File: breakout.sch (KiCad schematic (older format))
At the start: 20 parts, among them P1 CONN_01X08, P2 SPEAKER, P3 ISO7816_SIMPLE, P4 CONN_01X04, P5 SMA_CONN, P6 CONN_01X08, Q1 Q_PMOS_GSD, Q2 Q_NMOS_GSD, U1 SPX3819, U2 ESP-12E

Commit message: More stuff.
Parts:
- removed P4: CONN_01X04, Pin_Headers:Pin_Header_Straight_1x04, symbol CONN_01X04
- removed P6: CONN_01X08, Pin_Headers:Pin_Header_Straight_1x08, symbol CONN_01X08
- added J1: JACK_TRS_4PINS, Misc:PJ-320L, symbol JACK_TRS_4PINS
- added P4: CONN_01X09, Pin_Headers:Pin_Header_Straight_1x09, symbol CONN_01X09
- added P7: USB_A, Connect:USB_Micro-B_10103594-0001LF, symbol USB_A
- C3: value 470 uF -> 100 uF; footprint Capacitors_ThroughHole:C_Radial_D8_L13_P3.8 -> Capacitors_Tantalum_SMD:TantalC_SizeB_EIA-3528_HandSoldering
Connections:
- net labels added: ADC, CH_PD, EARL, EARR, GPIO0, GPIO12, GPIO13, GPIO14, GPIO16, GPIO2, GPIO4, GPIO5, MIC+, REST, RX, TX
- wire segments 147 -> 118
- no-connect marks 25 -> 27
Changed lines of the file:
@@
 LIBS:SIMtrace
 LIBS:smartcard
+LIBS:misc
+LIBS:nodemcu
+LIBS:sensors
 LIBS:breakout-cache
 EELAYER 25 0
@@
 P 6000 4850
 F 0 "C3" H 6025 4950 50  0000 L CNN
-F 1 "470 uF" H 6025 4750 50  0000 L CNN
-F 2 "Capacitors_ThroughHole:C_Radial_D8_L13_P3.8" H 6038 4700 50  0001 C CNN
+F 1 "100 uF" H 6025 4750 50  0000 L CNN
+F 2 "Capacitors_Tantalum_SMD:TantalC_SizeB_EIA-3528_HandSoldering" H 6038 4700 50  0001 C CNN
 F 3 "" H 6000 4850 50  0000 C CNN
 	1    6000 4850
@@
 NoConn ~ 2900 5550
 NoConn ~ 2900 5650
-$Comp
-L CONN_01X04 P4
-U 1 1 57B00DE5
-P 3750 7300
-F 0 "P4" H 3750 7550 50  0000 C CNN
-F 1 "CONN_01X04" V 3850 7300 50  0000 C CNN
-F 2 "Pin_Headers:Pin_Header_Straight_1x04" H 3750 7300 50  0001 C CNN
-F 3 "" H 3750 7300 50  0000 C CNN
-	1    3750 7300
-	0    1    1    0
-$EndComp
-NoConn ~ 2900 6350
 NoConn ~ 2900 6550
 $Comp
@@
 $EndComp
 $Comp
-L GND #PWR012
+L GND #PWR011
 U 1 1 57B7110B
 P 9000 4550
-F 0 "#PWR012" H 9000 4300 50  0001 C CNN
+F 0 "#PWR011" H 9000 4300 50  0001 C CNN
 F 1 "GND" H 9000 4400 50  0000 C CNN
 F 2 "" H 9000 4550 50  0000 C CNN
@@
 	1750 1350 1750 1250
 Wire Wire Line
-	4100 1750 4700 1750
-Wire Wire Line
-	4700 1750 4800 1750
-Wire Wire Line
-	4100 1950 4350 1950
-Wire Wire Line
-	4350 1950 4800 1950
-Wire Wire Line
-	4100 2150 4550 2150
-Wire Wire Line
-	4550 2150 4800 2150
-Wire Wire Line
-	4100 2250 4450 2250
-Wire Wire Line
-	4450 2250 4800 2250
-Wire Wire Line
-	6600 2150 6650 2150
-Wire Wire Line
-	6650 2150 7250 2150
-Wire Wire Line
-	6600 2250 7000 2250
-Wire Wire Line
-	7000 2250 7250 2250
-Wire Wire Line
-	6600 2350 6900 2350
-Wire Wire Line
-	6900 2350 7150 2350
-Wire Wire Line
-	7150 2350 7250 2350
+	4100 1750 4800 1750
+Wire Wire Line
+	4100 1950 4800 1950
+Wire Wire Line
+	4100 2150 4800 2150
+Wire Wire Line
+	4100 2250 4800 2250
+Wire Wire Line
+	6600 2150 7250 2150
+Wire Wire Line
+	6600 2250 7250 2250
+Wire Wire Line
+	6600 2350 7250 2350
 Wire Wire Line
 	6600 2450 6650 2450
 Wire Wire Line
-	3650 950  3850 950
-Wire Wire Line
-	3850 950  4200 950
-Wire Wire Line
-	4200 950  4350 950
-Wire Wire Line
-	4350 950  4700 950
-Wire Wire Line
-	4700 950  6650 950
-Wire Wire Line
-	6650 950  7000 950
-Wire Wire Line
-	3200 1300 3200 1550
-Wire Wire Line
-	3200 1550 3200 3050
-Wire Wire Line
-	3200 3050 6650 3050
-Wire Wire Line
-	6650 3050 6900 3050
-Wire Wire Line
-	6900 3050 7250 3050
+	3650 950  7000 950
+Wire Wire Line
+	3200 1300 3200 3050
+Wire Wire Line
+	2400 3050 7250 3050
 Wire Wire Line
 	4350 1450 4350 1950
@@
 	5650 5150 5400 5150
 Wire Wire Line
-	5400 4850 5650 4850
-Wire Wire Line
-	5650 4850 5850 4850
+	5400 4850 5850 4850
 Wire Wire Line
 	5400 4750 5650 4750
@@
 	5650 4650 5650 4550
 Wire Wire Line
-	5400 4550 5650 4550
-Wire Wire Line
-	5650 4550 6200 4550
-Wire Wire Line
-	6200 4550 6300 4550
+	5400 4550 6300 4550
 Wire Wire Line
 	6200 4550 6200 4850
@@
 Connection ~ 5650 6550
 Wire Wire Line
-	2500 5000 2500 5100
-Wire Wire Line
-	2500 5100 2500 5750
-Wire Wire Line
-	2500 5750 2500 6250
-Wire Wire Line
-	2500 6250 2500 6350
+	2500 5000 2500 6350
 Wire Wire Line
 	2500 5750 2900 5750
@@
 Wire Wire Line
 	6100 5250 5400 5250
-Wire Wire Line
-	3700 7100 3700 6850
-Wire Wire Line
-	3700 6850 5450 6850
-Wire Wire Line
-	5450 6850 5450 6650
-Wire Wire Line
-	5650 6650 5450 6650
-Connection ~ 5650 6650
-Wire Wire Line
-	5400 6350 5550 6350
-Wire Wire Line
-	5550 6350 5550 6950
-Wire Wire Line
-	5550 6950 3800 6950
-Wire Wire Line
-	3800 6950 3800 7100
-Wire Wire Line
-	3900 7100 5600 7100
-Wire Wire Line
-	5600 7100 5600 6450
-Wire Wire Line
-	5600 6450 5400 6450
-Wire Wire Line
-	3600 7100 2800 7100
-Wire Wire Line
-	2800 7100 2800 6450
-Wire Wire Line
-	2800 6450 2900 6450
 Wire Wire Line
 	1000 5200 1000 5200
@@
 	6100 5350 6100 5400
 Wire Wire Line
-	5650 4750 5650 4850
-Wire Wire Line
-	5650 4850 5650 5150
-Wire Wire Line
-	5650 5150 5650 5350
-Wire Wire Line
-	5650 5350 5650 5950
-Wire Wire Line
-	5650 5950 5650 6250
-Wire Wire Line
-	5650 6250 5650 6550
-Wire Wire Line
-	5650 6550 5650 6650
-Wire Wire Line
-	5650 6650 5650 7150
+	5650 4750 5650 7150
 Wire Wire Line
 	7250 3050 7250 2450
 Wire Wire Line
-	2500 6250 2900 6250
+	2300 6250 2900 6250
 Wire Wire Line
 	2900 5250 2850 5250
@@
 	5400 6150 5850 6150
 Wire Wire Line
-	2650 850  2650 950
-Wire Wire Line
-	2650 950  2650 1100
-Wire Wire Line
-	2650 1100 2650 2600
+	2650 850  2650 2600
 Wire Wire Line
 	2650 950  2750 950
@@
 Connection ~ 7150 2350
 Wire Wire Line
-	9450 3550 9450 3600
-Wire Wire Line
-	9450 3600 9450 3750
+	9450 3550 9450 3750
 Wire Wire Line
 	9450 3600 9000 3600
 Connection ~ 9450 3600
 Wire Wire Line
-	9000 3900 9000 3950
-Wire Wire Line
-	9000 3950 9000 4050
+	9000 3900 9000 4050
 Wire Wire Line
 	9000 3950 9150 3950
@@
 Wire Wire Line
 	9450 4250 9850 4250
-$Comp
-L CONN_01X08 P6
-U 1 1 57B536C2
-P 3900 2100
-F 0 "P6" H 3900 2550 50  0000 C CNN
-F 1 "CONN_01X08" V 4000 2100 50  0000 C CNN
-F 2 "Pin_Headers:Pin_Header_Straight_1x08" H 3900 2100 50  0001 C CNN
-F 3 "" H 3900 2100 50  0000 C CNN
-	1    3900 2100
+Wire Wire Line
+	2650 2600 4100 2600
+Connection ~ 2650 1100
+$Comp
+L USB_A P7
+U 1 1 57B79205
+P 1800 1950
+F 0 "P7" H 2000 1750 50  0000 C CNN
+F 1 "USB_A" H 1750 2150 50  0000 C CNN
+F 2 "Connect:USB_Micro-B_10103594-0001LF" V 1750 1850 50  0001 C CNN
+F 3 "" V 1750 1850 50  0000 C CNN
+	1    1800 1950
+	0    -1   -1   0
+$EndComp
+Wire Wire Line
+	2100 2150 2650 2150
+Connection ~ 2650 2150
+Wire Wire Line
+	2100 1850 2400 1850
+Wire Wire Line
+	2400 1850 2400 3050
+Connection ~ 3200 3050
+NoConn ~ 2100 1950
+NoConn ~ 2100 2050
+NoConn ~ 1700 1650
+Wire Wire Line
+	2900 6350 2850 6350
+Wire Wire Line
+	2850 6350 2850 6250
+Connection ~ 2850 6250
+$Comp
+L JACK_TRS_4PINS J1
+U 1 1 57B7BE51
+P 1650 7250
+F 0 "J1" H 1650 7650 50  0000 C CNN
+F 1 "JACK_TRS_4PINS" H 1600 6950 50  0000 C CNN
+F 2 "Misc:PJ-320L" H 1750 7100 50  0001 C CNN
+F 3 "" H 1750 7100 50  0000 C CNN
+	1    1650 7250
+	1    0    0    -1
+$EndComp
+Wire Wire Line
+	2900 6450 2750 6450
+Wire Wire Line
+	2750 6450 2750 6950
+Wire Wire Line
+	2750 6950 2150 6950
+Wire Wire Line
+	2150 7050 2300 7050
+Wire Wire Line
+	2300 7050 2300 6250
+Wire Wire Line
+	5400 6450 5450 6450
+Wire Wire Line
+	5450 6450 5450 7250
+Wire Wire Line
+	5450 7250 2150 7250
+Wire Wire Line
+	2150 7450 5550 7450
+Wire Wire Line
+	5550 7450 5550 6350
+Wire Wire Line
+	5550 6350 5400 6350
+$Comp
+L CONN_01X09 P4
+U 1 1 57B7BAFE
+P 3900 2150
+F 0 "P4" H 3900 2650 50  0000 C CNN
+F 1 "CONN_01X09" V 4000 2150 50  0000 C CNN
+F 2 "Pin_Headers:Pin_Header_Straight_1x09" H 3900 2150 50  0001 C CNN
+F 3 "" H 3900 2150 50  0000 C CNN
+	1    3900 2150
 	-1   0    0    -1
 $EndComp
 Wire Wire Line
-	4100 2450 4100 2600
-Wire Wire Line
-	4100 2600 2650 2600
-Connection ~ 2650 1100
+	4100 2600 4100 2550
+Wire Wire Line
+	4100 2450 4150 2450
+Wire Wire Line
+	4150 2450 4150 3050
+Connection ~ 4150 3050
+Text Label 6750 1750 0    39   ~ 0
+TX
+Text Label 6750 1850 0    39   ~ 0
+RX
+Text Label 6750 1950 0    39   ~ 0
+GPIO5
+Text Label 6750 2050 0    39   ~ 0
+GPIO4
+Text Label 6750 2150 0    39   ~ 0
+GPIO0
+Text Label 6750 2250 0    39   ~ 0
+GPIO2
+Text Label 4500 1750 0    39   ~ 0
+REST
+Text Label 4500 1850 0    39   ~ 0
+ADC
+Text Label 4500 1950 0    39   ~ 0
+CH_PD
+Text Label 4500 2050 0    39   ~ 0
+GPIO16
+Text Label 4500 2150 0    39   ~ 0
+GPIO14
+Text Label 2450 6950 0    39   ~ 0
+MIC+
+Text Label 2450 7250 0    39   ~ 0
+EARL
+Text Label 2450 7450 0    39   ~ 0
+EARR
+Text Label 4500 2250 0    39   ~ 0
+GPIO12
+Text Label 4500 2350 0    39   ~ 0
+GPIO13
 $EndSCHEMATC

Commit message: More stuff.
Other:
- note removed: "TODO:\n* Add input barrel jack.\n* Check the audio connections.\n* Check the SIM card holder dimensions.\n* Check the SMA antenna dimensions."
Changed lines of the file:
@@
 	0    1    1    0
 $EndComp
-Text Notes 8650 950  0    60   ~ 0
-TODO:\n* Add input barrel jack.\n* Check the audio connections.\n* Check the SIM card holder dimensions.\n* Check the SMA antenna dimensions.
 NoConn ~ 2900 4550
 NoConn ~ 2900 4650

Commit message: Add LED.
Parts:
- added D1: LED, LEDs:LED_0805, symbol LED
- added R7: 150Ω, Resistors_SMD:R_0805_HandSoldering, symbol R
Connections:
- net GND: now also R7.2
- net VBAT: now also D1.2 (A)
- new net: D1.1 (K), R7.1
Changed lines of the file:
@@
 Text Label 4500 2350 0    39   ~ 0
 GPIO13
+$Comp
+L LED D1
+U 1 1 57BA1DA8
+P 9750 4550
+F 0 "D1" H 9750 4650 50  0000 C CNN
+F 1 "LED" H 9750 4450 50  0000 C CNN
+F 2 "LEDs:LED_0805" H 9750 4550 50  0001 C CNN
+F 3 "" H 9750 4550 50  0000 C CNN
+	1    9750 4550
+	0    -1   -1   0
+$EndComp
+$Comp
+L GND #PWR012
+U 1 1 57BA1E9B
+P 9750 5250
+F 0 "#PWR012" H 9750 5000 50  0001 C CNN
+F 1 "GND" H 9750 5100 50  0000 C CNN
+F 2 "" H 9750 5250 50  0000 C CNN
+F 3 "" H 9750 5250 50  0000 C CNN
+	1    9750 5250
+	1    0    0    -1
+$EndComp
+$Comp
+L R R7
+U 1 1 57BA2411
+P 9750 5000
+F 0 "R7" H 9820 5046 50  0000 L CNN
+F 1 "150Ω" H 9820 4954 50  0000 L CNN
+F 2 "Resistors_SMD:R_0805_HandSoldering" V 9680 5000 50  0001 C CNN
+F 3 "" H 9750 5000 50  0000 C CNN
+	1    9750 5000
+	1    0    0    -1
+$EndComp
+Wire Wire Line
+	9750 4250 9750 4350
+Connection ~ 9750 4250
+Wire Wire Line
+	9750 5150 9750 5250
+Wire Wire Line
+	9750 4750 9750 4850
 $EndSCHEMATC

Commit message: Various updates.
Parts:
- P3: footprint smartcard:SIM_LIGHT -> Misc:SIM_115C_AC00_R
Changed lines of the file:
@@
 F 0 "P3" H 1550 5300 60  0000 C CNN
 F 1 "ISO7816_SIMPLE" H 1550 4900 60  0000 C CNN
-F 2 "smartcard:SIM_LIGHT" H 1550 5100 60  0001 C CNN
+F 2 "Misc:SIM_115C_AC00_R" H 1550 5100 60  0001 C CNN
 F 3 "" H 1550 5100 60  0001 C CNN
 	1    1550 5100

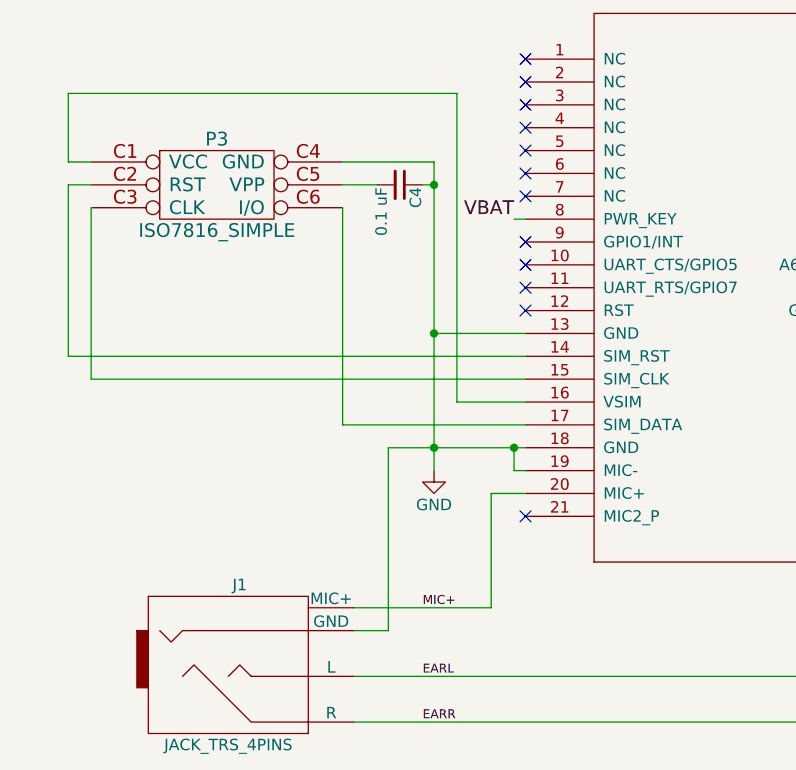
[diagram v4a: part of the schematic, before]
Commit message: Add microphone output.
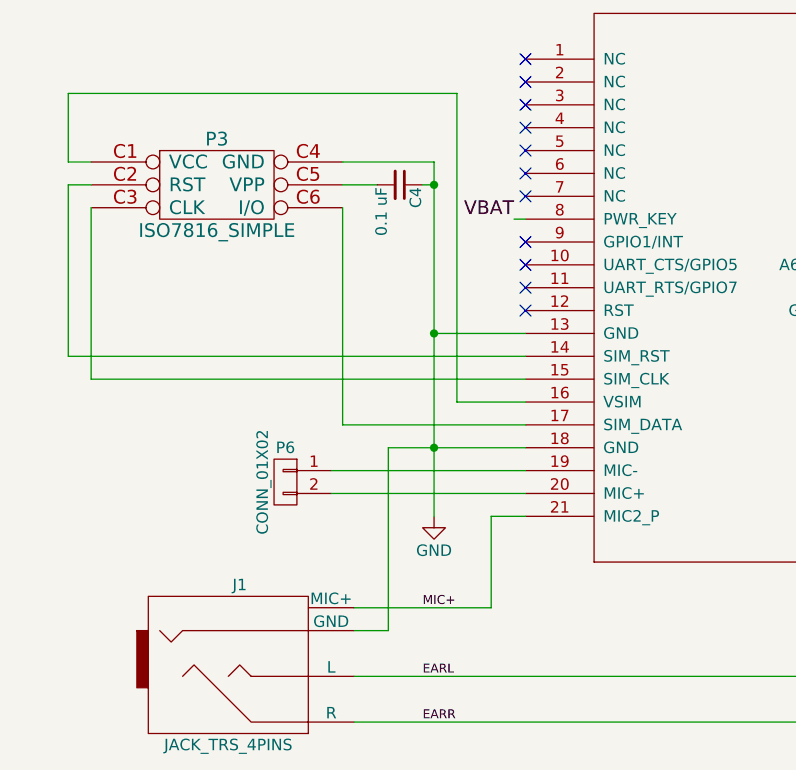
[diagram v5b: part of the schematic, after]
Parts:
- added P6: CONN_01X02, Pin_Headers:Pin_Header_Straight_1x02, symbol CONN_01X02
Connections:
- net GND: no longer GSM1.19 (MIC-)
- net MIC+: now also GSM1.21 (MIC2_P); no longer GSM1.20 (MIC+)
- new net: GSM1.19 (MIC-), P6.1 (P1)
- new net: GSM1.20 (MIC+), P6.2 (P2)
- no-connect marks 27 -> 26
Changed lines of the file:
@@
 NoConn ~ 2900 5550
 NoConn ~ 2900 5650
-NoConn ~ 2900 6550
 $Comp
 L ISO7816_SIMPLE P3
@@
 L GND #PWR07
 U 1 1 57B4FD98
-P 2500 6350
-F 0 "#PWR07" H 2500 6100 50  0001 C CNN
-F 1 "GND" H 2500 6200 50  0000 C CNN
-F 2 "" H 2500 6350 50  0000 C CNN
-F 3 "" H 2500 6350 50  0000 C CNN
-	1    2500 6350
+P 2500 6550
+F 0 "#PWR07" H 2500 6300 50  0001 C CNN
+F 1 "GND" H 2500 6400 50  0000 C CNN
+F 2 "" H 2500 6550 50  0000 C CNN
+F 3 "" H 2500 6550 50  0000 C CNN
+	1    2500 6550
 	1    0    0    -1
 $EndComp
@@
 Connection ~ 5650 6550
 Wire Wire Line
-	2500 5000 2500 6350
+	2500 5000 2500 6550
 Wire Wire Line
 	2500 5750 2900 5750
@@
 NoConn ~ 2100 2050
 NoConn ~ 1700 1650
-Wire Wire Line
-	2900 6350 2850 6350
-Wire Wire Line
-	2850 6350 2850 6250
-Connection ~ 2850 6250
 $Comp
 L JACK_TRS_4PINS J1
@@
 	1    0    0    -1
 $EndComp
-Wire Wire Line
-	2900 6450 2750 6450
-Wire Wire Line
-	2750 6450 2750 6950
 Wire Wire Line
 	2750 6950 2150 6950
@@
 Wire Wire Line
 	9750 4750 9750 4850
+Wire Wire Line
+	2750 6950 2750 6550
+Wire Wire Line
+	2750 6550 2900 6550
+$Comp
+L CONN_01X02 P6
+U 1 1 57BA60E6
+P 1850 6400
+F 0 "P6" H 1850 6550 50  0000 C CNN
+F 1 "CONN_01X02" V 1950 6400 50  0000 C CNN
+F 2 "Pin_Headers:Pin_Header_Straight_1x02" H 1850 6400 50  0001 C CNN
+F 3 "" H 1850 6400 50  0000 C CNN
+	1    1850 6400
+	-1   0    0    -1
+$EndComp
+Wire Wire Line
+	2050 6350 2900 6350
+Wire Wire Line
+	2900 6450 2050 6450
 $EndSCHEMATC

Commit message: Add a bunch of audio crap.
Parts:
- added C1, C10, C11, C5, C9: 33uF, Capacitors_SMD:C_0805_HandSoldering, symbol C
- added C6, C7, C8: 10uF, Capacitors_SMD:C_0805_HandSoldering, symbol C
- added R8: 68Ω, Resistors_SMD:R_0805_HandSoldering, symbol R
- P6: value CONN_01X02 -> MIC
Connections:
- net EARL: now also C10.2, C6.1, C7.2, C9.1
- net EARR: now also C10.1, C11.2, C7.1, C8.2
- net GND: now also C1.2, C11.1, C5.2, C6.2, C8.1, C9.2
- net GPIO12 renamed ESP_TX
- net GPIO14 renamed ESP_RX
- net MIC+: no longer names the net of J1.5 (MIC+)
- net MIC+: now also C5.1, R8.2; no longer GSM1.21 (MIC2_P)
- new net MIC2_P: C1.1, GSM1.21 (MIC2_P), R8.1
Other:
- note added: "A6"
- note added: "Audio"
- note added: "ESP8266"
- note added: "Power control"
- note added: "SIM"
- moved on the sheet: C2, C3, C4, D1, GSM1, J1, P1, P2, P3, P4, P5, P6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

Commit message: Add inductors for audio.
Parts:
- added L1, L2, L3, L4: 68nH, Resistors_SMD:R_0805_HandSoldering, symbol L_Small
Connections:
- net at GSM1.19 (MIC-): now also L1.1; no longer P6.1 (P1)
- net at GSM1.20 (MIC+): now also L2.1; no longer P6.2 (P2)
- net at GSM1.26 (REC+): now also L4.2; no longer P2.2 (P2)
- net at GSM1.27 (REC-): now also L3.2; no longer P2.1 (P1)
- new net: L3.1, P2.1 (P1)
- new net: L4.1, P2.2 (P2)
- new net: L1.2, P6.1 (P1)
- new net: L2.2, P6.2 (P2)
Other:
- moved on the sheet: P2
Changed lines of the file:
@@
 L CONN_01X02 P2
 U 1 1 57B508A2
-P 6200 6450
-F 0 "P2" H 6200 6600 50  0000 C CNN
-F 1 "SPEAKER" V 6300 6450 50  0000 C CNN
-F 2 "Pin_Headers:Pin_Header_Straight_1x02" H 6200 6450 50  0001 C CNN
-F 3 "" H 6200 6450 50  0000 C CNN
-	1    6200 6450
+P 6550 6450
+F 0 "P2" H 6550 6600 50  0000 C CNN
+F 1 "SPEAKER" V 6650 6450 50  0000 C CNN
+F 2 "Pin_Headers:Pin_Header_Straight_1x02" H 6550 6450 50  0001 C CNN
+F 3 "" H 6550 6450 50  0000 C CNN
+	1    6550 6450
 	1    0    0    -1
 $EndComp
@@
 Connection ~ 3150 1250
 Wire Wire Line
-	5100 3350 5100 2750
+	5100 2750 5100 3350
 Wire Wire Line
 	5350 2650 5350 2850
@@
 	3050 5600 3000 5600
 Wire Wire Line
-	5550 6400 6000 6400
-Wire Wire Line
-	5550 6500 6000 6500
+	5550 6400 6050 6400
+Wire Wire Line
+	5550 6500 6050 6500
 Wire Wire Line
 	1100 1150 1100 2950
@@
 Wire Wire Line
 	8350 3300 8600 3300
-Wire Wire Line
-	2200 6700 3050 6700
-Wire Wire Line
-	3050 6800 2200 6800
 Wire Wire Line
 	8500 3300 8500 3350
@@
 Text Notes 1600 5000 0    118  ~ 24
 SIM
+$Comp
+L L_Small L1
+U 1 1 57BB2439
+P 2450 6700
+F 0 "L1" V 2500 6550 50  0000 L CNN
+F 1 "68nH" V 2500 6700 50  0000 L CNN
+F 2 "Resistors_SMD:R_0805_HandSoldering" H 2450 6700 50  0001 C CNN
+F 3 "" H 2450 6700 50  0000 C CNN
+	1    2450 6700
+	0    1    1    0
+$EndComp
+Wire Wire Line
+	2200 6700 2350 6700
+Wire Wire Line
+	2550 6700 3050 6700
+$Comp
+L L_Small L2
+U 1 1 57BB29AA
+P 2450 6800
+F 0 "L2" V 2500 6650 50  0000 L CNN
+F 1 "68nH" V 2500 6800 50  0000 L CNN
+F 2 "Resistors_SMD:R_0805_HandSoldering" H 2450 6800 50  0001 C CNN
+F 3 "" H 2450 6800 50  0000 C CNN
+	1    2450 6800
+	0    1    1    0
+$EndComp
+Wire Wire Line
+	2200 6800 2350 6800
+Wire Wire Line
+	2550 6800 3050 6800
+$Comp
+L L_Small L4
+U 1 1 57BB3843
+P 6150 6500
+F 0 "L4" V 6200 6350 50  0000 L CNN
+F 1 "68nH" V 6200 6500 50  0000 L CNN
+F 2 "Resistors_SMD:R_0805_HandSoldering" H 6150 6500 50  0001 C CNN
+F 3 "" H 6150 6500 50  0000 C CNN
+	1    6150 6500
+	0    1    1    0
+$EndComp
+$Comp
+L L_Small L3
+U 1 1 57BB3A0F
+P 6150 6400
+F 0 "L3" V 6200 6250 50  0000 L CNN
+F 1 "68nH" V 6200 6400 50  0000 L CNN
+F 2 "Resistors_SMD:R_0805_HandSoldering" H 6150 6400 50  0001 C CNN
+F 3 "" H 6150 6400 50  0000 C CNN
+	1    6150 6400
+	0    1    1    0
+$EndComp
+Wire Wire Line
+	6250 6400 6350 6400
+Wire Wire Line
+	6250 6500 6350 6500
 $EndSCHEMATC

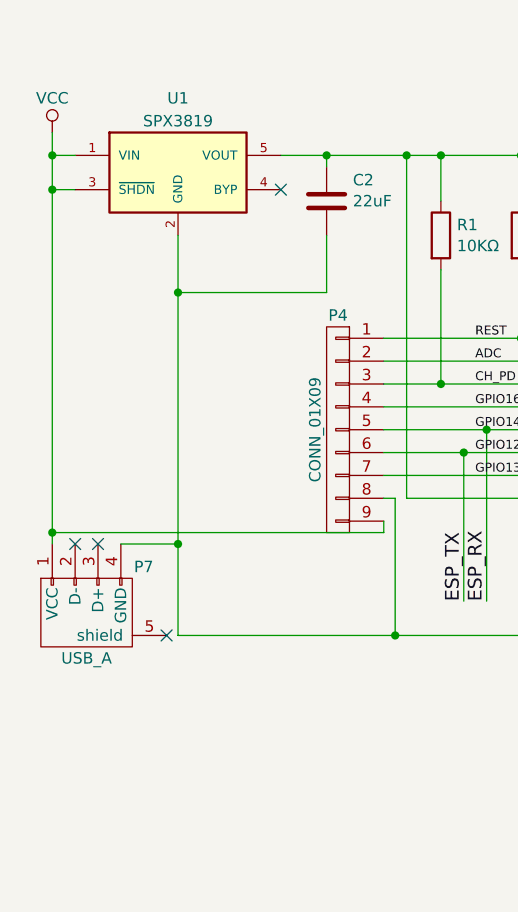
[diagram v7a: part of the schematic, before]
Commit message: Fix USB pin issue.
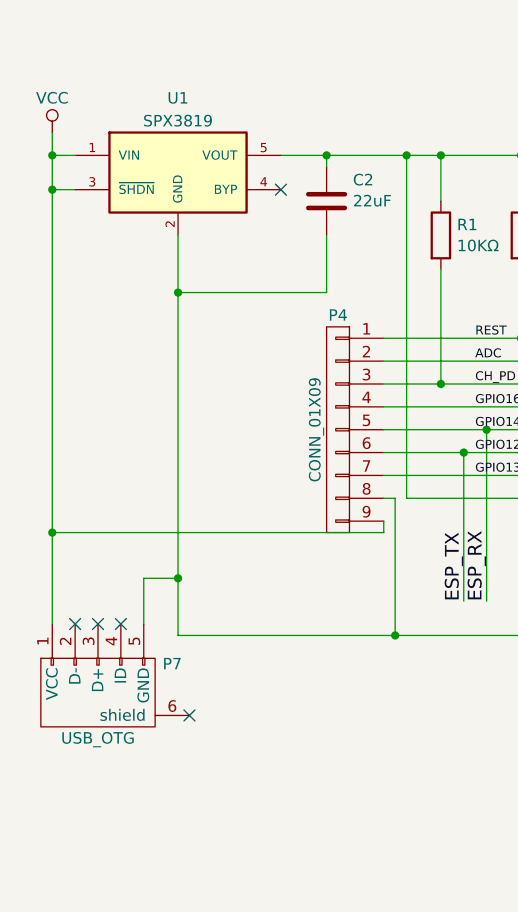
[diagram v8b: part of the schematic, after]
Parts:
- removed P7: USB_A, Connect:USB_Micro-B_10103594-0001LF, symbol USB_A
- added P7: USB_OTG, Connect:USB_Micro-B_10103594-0001LF, symbol USB_OTG
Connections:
- net GND: now also P7.5 (GND)
- net VCC: now also P7.1 (VCC)
- no-connect marks 26 -> 27
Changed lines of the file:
@@
 Text Label 10800 1850 0    60   ~ 0
 VBAT
-$Comp
-L USB_A P7
-U 1 1 57B79205
-P 1300 3250
-F 0 "P7" H 1500 3050 50  0000 C CNN
-F 1 "USB_A" H 1250 3450 50  0000 C CNN
-F 2 "Connect:USB_Micro-B_10103594-0001LF" V 1250 3150 50  0001 C CNN
-F 3 "" V 1250 3150 50  0000 C CNN
-	1    1300 3250
-	1    0    0    1
-$EndComp
-NoConn ~ 1300 2950
-NoConn ~ 1200 2950
-NoConn ~ 1600 3350
+NoConn ~ 1300 3300
+NoConn ~ 1200 3300
 $Comp
 L JACK_TRS_4PINS J1
@@
 	5550 6500 6050 6500
 Wire Wire Line
-	1100 1150 1100 2950
-Wire Wire Line
 	1100 1250 1200 1250
 Wire Wire Line
@@
 	1650 3350 5700 3350
 Connection ~ 1100 2900
-Wire Wire Line
-	1400 2950 1650 2950
-Connection ~ 1650 2950
 Wire Wire Line
 	7550 4350 8700 4350
@@
 Wire Wire Line
 	6250 6500 6350 6500
+$Comp
+L USB_OTG P7
+U 1 1 57DB372C
+P 1300 3600
+F 0 "P7" H 1625 3475 50  0000 C CNN
+F 1 "USB_OTG" H 1300 3800 50  0000 C CNN
+F 2 "Connect:USB_Micro-B_10103594-0001LF" V 1250 3500 50  0001 C CNN
+F 3 "" V 1250 3500 50  0000 C CNN
+	1    1300 3600
+	1    0    0    1
+$EndComp
+NoConn ~ 1700 3700
+Wire Wire Line
+	1500 3300 1500 3100
+Wire Wire Line
+	1500 3100 1650 3100
+Connection ~ 1650 3100
+Wire Wire Line
+	1100 1150 1100 3300
+NoConn ~ 1400 3300
 $EndSCHEMATC
